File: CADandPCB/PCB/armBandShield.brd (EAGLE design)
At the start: 26.1 x 55.9 mm, 33 parts, among them J1 FSR_HEADERS_1, J2 FSR_HEADERS_2, Q1 BSS138, Q2 BSS138, U2 MPU-6050-1

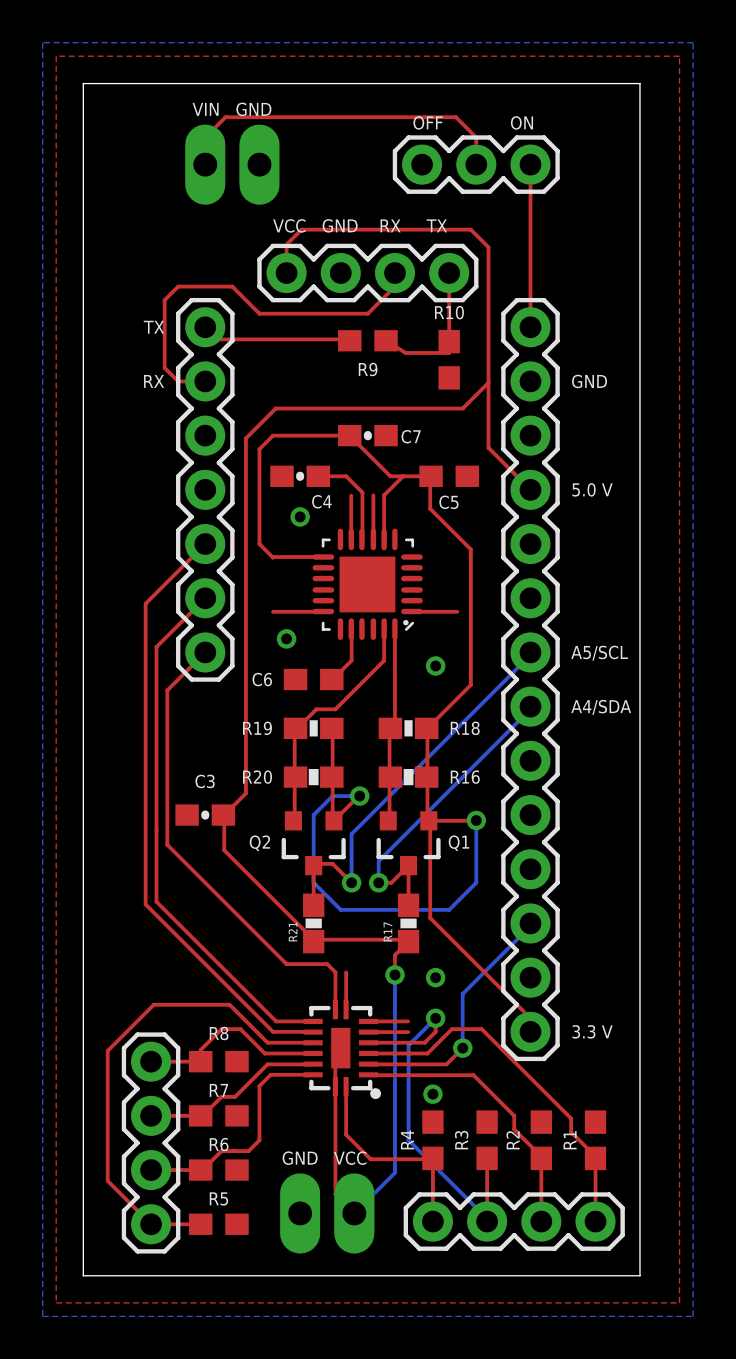
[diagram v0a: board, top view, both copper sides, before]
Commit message: Update trace sizes, pad extensions, silkscreen, and some routing.
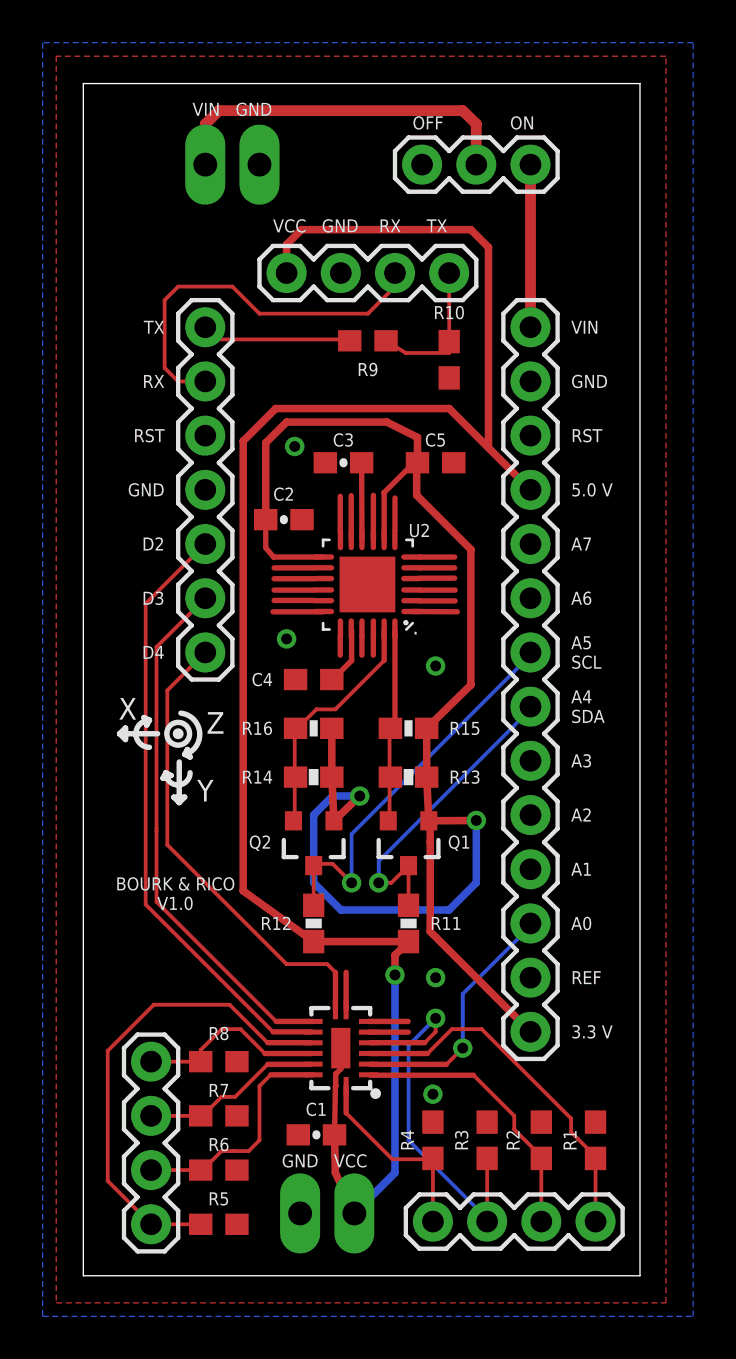
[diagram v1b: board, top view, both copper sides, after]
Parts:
- removed C6: 2.2nF, SparkFun-Capacitors:0603
- removed C7: 0.1uF, SparkFun-Capacitors:0603-CAP
- removed R19: 10K, SparkFun-Resistors:0603-RES
- added C1, C2: 0.1uF, SparkFun-Capacitors:0603-CAP
- added R13: 10K, SparkFun:0603-RES
- C4: value 0.1uF -> 2.2nF; device SparkFun-Capacitors:0603-CAP -> SparkFun-Capacitors:0603
- R16: device SparkFun:0603-RES -> SparkFun-Resistors:0603-RES
- moved C3 17.7 mm to (12.2, 38.1)
- moved C4 9.55 mm to (10.8, 27.9)
- moved R16 5.00 mm to (10.8, 25.7)
- moved C5 0.90 mm to (16.5, 38.1)
- renumbered R17 to R11, R18 to R15, R20 to R14, R21 to R12
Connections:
- net A4/SDA/LOW: now also R13.2; no longer R16.2
- net A5/SCL/LOW: now also R16.2; no longer R19.2
- net GND: now also C1.2, C2.2; no longer C6.2, C7.2
- net N$3: now also C4.1; no longer C6.1
- net N$5: now also C3.1; no longer C4.1
- net VCC: now also C1.1; no longer C3.1
- net VCC_2: now also C2.1, R13.1; no longer C7.1, R19.1
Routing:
- net VCC_2: track 75.6 -> 78.0 mm
- net N$9: track 0.00 -> 1.91 mm
- net N$8: track 0.00 -> 1.91 mm
- net N$6: track 0.00 -> 1.91 mm
- net N$4: track 0.00 -> 1.91 mm
- net N$16: track 0.00 -> 1.65 mm
- net N$15: track 0.00 -> 1.65 mm
- net N$14: track 0.00 -> 1.65 mm
- net N$17: track 0.00 -> 1.65 mm
- net N$13: track 0.00 -> 1.65 mm
- net N$19: track 0.00 -> 1.65 mm
- net N$18: track 0.00 -> 1.52 mm
- net N$5: track 4.59 -> 3.59 mm
- net N$1: track 16.0 -> 17.0 mm
- net N$12: track 0.00 -> 0.89 mm
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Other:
- board text added: "."
- board text added: "A0"
- board text added: "A1"
- board text added: "A2"
- board text added: "A3"
- board text added: "A4 SDA"
- board text added: "A5 SCL"
- board text added: "A6"
- board text added: "A7"
- board text added: "BOURK & RICO V1.0"
- board text added: "D2"
- board text added: "D3"
- board text added: "D4"
- board text added: "REF"
- board text added: "RST"
- board text added: "U2"
- board text added: "VIN"
- board text added: "X"
- board text added: "Y"
- board text added: "Z"
- board text removed: "A4/SDA"
- board text removed: "A5/SCL"

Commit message: Double checked schematic and moved a few traces for asthetics.
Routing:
- net VCC: track 88.3 -> 93.4 mm
- net VCC_2: track 78.0 -> 77.1 mm
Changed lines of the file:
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@@
 <circle x="4.445" y="25.4" radius="0.127" width="0.254" layer="21"/>
 <circle x="4.445" y="25.4" radius="0.5334" width="0.254" layer="21"/>
-<text x="4.318" y="17.145" size="0.6096" layer="25" font="vector" ratio="20" align="bottom-center">BOURK &amp; RICO
+<text x="3.683" y="14.605" size="0.6096" layer="25" font="vector" ratio="20" align="bottom-center">BOURK &amp; RICO
 V1.0</text>
 <text x="15.5702" y="30.4292" size="0.762" layer="25" font="vector" ratio="20" align="center">.</text>
@@
 <wire x1="13.5925" y1="34.5066" x2="13.5925" y2="36.5725" width="0.254" layer="1"/>
 <wire x1="12.5554" y1="34.5066" x2="12.5554" y2="36.5584" width="0.254" layer="1"/>
-<via x="16.383" y="8.509" extent="1-16" drill="0.508"/>
-<via x="16.51" y="13.97" extent="1-16" drill="0.508"/>
+<via x="17.653" y="8.509" extent="1-16" drill="0.508"/>
+<via x="15.24" y="13.97" extent="1-16" drill="0.508"/>
 <wire x1="11.2355" y1="31.115" x2="8.89" y2="31.115" width="0.254" layer="1"/>
 <contactref element="U2" pad="9"/>
@@
 <wire x1="9.525" y1="48.3235" x2="9.525" y2="46.99" width="0.3556" layer="1"/>
 <wire x1="7.493" y1="18.034" x2="7.493" y2="39.116" width="0.3556" layer="1"/>
-<wire x1="14.605" y1="14.097" x2="14.605" y2="4.826" width="0.3556" layer="16"/>
-<wire x1="14.605" y1="4.826" x2="12.7" y2="2.921" width="0.3556" layer="16"/>
-<wire x1="14.605" y1="15.025" x2="14.605" y2="14.097" width="0.3556" layer="1"/>
-<via x="14.605" y="14.097" extent="1-16" drill="0.508"/>
+<via x="7.493" y="18.034" extent="1-16" drill="0.508"/>
 <wire x1="20.955" y1="36.83" x2="18.9865" y2="38.7985" width="0.3556" layer="1"/>
 <wire x1="18.9865" y1="38.7985" x2="17.145" y2="40.64" width="0.3556" layer="1"/>
@@
 <wire x1="17.145" y1="40.64" x2="9.017" y2="40.64" width="0.3556" layer="1"/>
 <wire x1="18.9865" y1="38.7985" x2="18.9865" y2="48.1965" width="0.3556" layer="1"/>
-<wire x1="10.795" y1="15.66" x2="7.493" y2="18.034" width="0.3556" layer="1"/>
-<wire x1="11.9086" y1="6.7406" x2="11.772" y2="6.604" width="0.3556" layer="1"/>
-<wire x1="11.772" y1="6.604" x2="11.7816" y2="6.763109375" width="0.3556" layer="1"/>
 <wire x1="10.795" y1="15.66" x2="15.24" y2="15.66" width="0.3556" layer="1"/>
-<wire x1="15.24" y1="15.66" x2="14.605" y2="15.025" width="0.3556" layer="1"/>
 <wire x1="12.7" y1="2.921" x2="11.811" y2="4.826" width="0.3556" layer="1"/>
 <wire x1="11.811" y1="4.826" x2="11.772" y2="6.604" width="0.3556" layer="1"/>
@@
 <wire x1="12.065" y1="9.69089375" x2="11.8324" y2="9.45829375" width="0.254" layer="1"/>
 <wire x1="11.8324" y1="9.45829375" x2="11.8324" y2="8.8854" width="0.254" layer="1"/>
+<wire x1="7.493" y1="18.034" x2="10.795" y2="15.66" width="0.3556" layer="1"/>
+<wire x1="7.493" y1="18.034" x2="14.6304" y2="12.9286" width="0.3556" layer="16"/>
+<wire x1="14.6304" y1="12.9286" x2="14.605" y2="6.35" width="0.3556" layer="16"/>
+<wire x1="14.605" y1="6.35" x2="12.7" y2="2.921" width="0.3556" layer="16"/>
 </signal>
 <signal name="RX">
@@
 <contactref element="RIGHT_HEADER" pad="1"/>
 <wire x1="16.256" y1="16.129" x2="20.955" y2="11.43" width="0.3556" layer="1"/>
-<wire x1="16.256" y1="21.209" x2="16.256" y2="20.32" width="0.3556" layer="1"/>
-<wire x1="16.256" y1="20.32" x2="16.256" y2="16.129" width="0.3556" layer="1"/>
+<wire x1="16.256" y1="16.129" x2="16.256" y2="20.32" width="0.3556" layer="1"/>
 <wire x1="15.494" y1="38.1" x2="15.66" y2="38.1" width="0.254" layer="1"/>
 <wire x1="18.161" y1="34.036" x2="15.621" y2="36.576" width="0.3556" layer="1"/>
@@
 <wire x1="16.19" y1="21.32" x2="16.09" y2="23.368" width="0.3556" layer="1"/>
 <wire x1="16.19" y1="21.32" x2="18.415" y2="21.336" width="0.3556" layer="1"/>
-<wire x1="16.19" y1="21.32" x2="16.256" y2="20.32" width="0.254" layer="1"/>
+<wire x1="16.256" y1="20.32" x2="16.19" y2="21.32" width="0.3556" layer="1"/>
 </signal>
 <signal name="A5/SCL/HIGH">

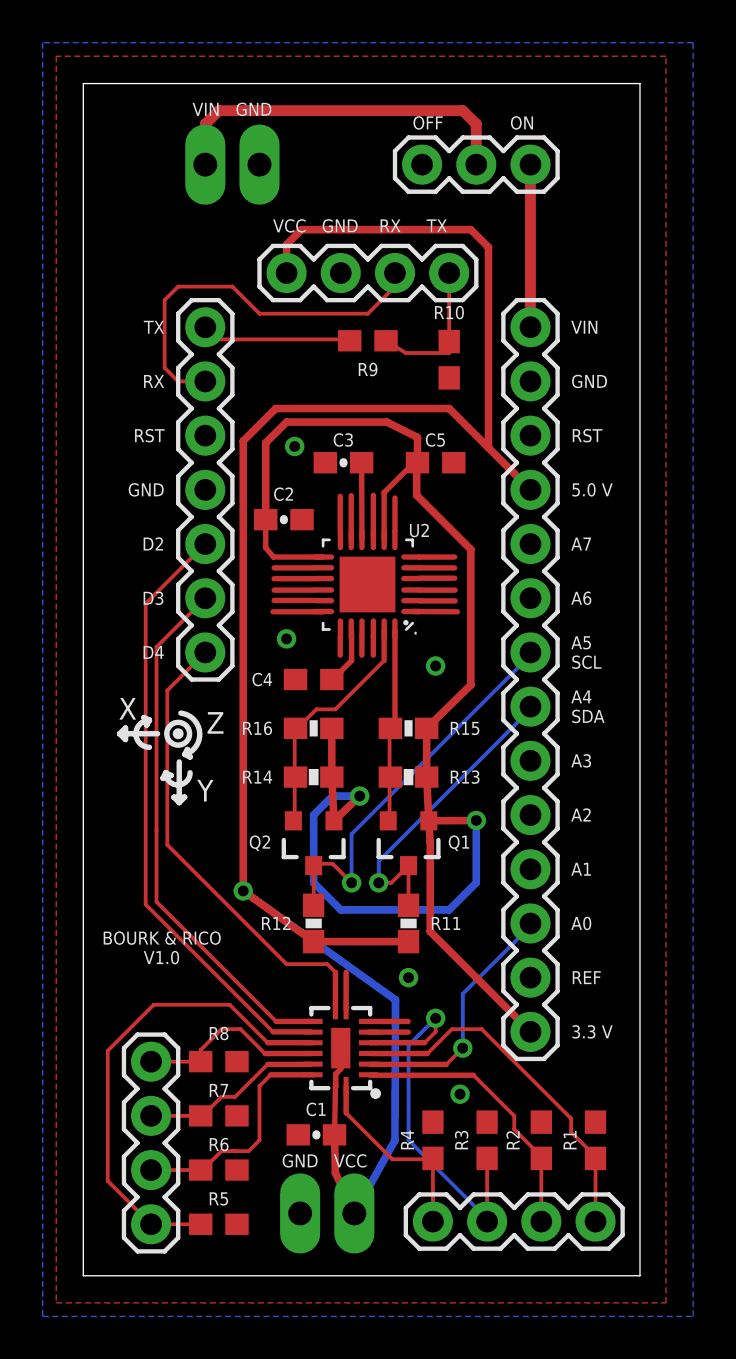
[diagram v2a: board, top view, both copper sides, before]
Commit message: Increase tstop and tcream
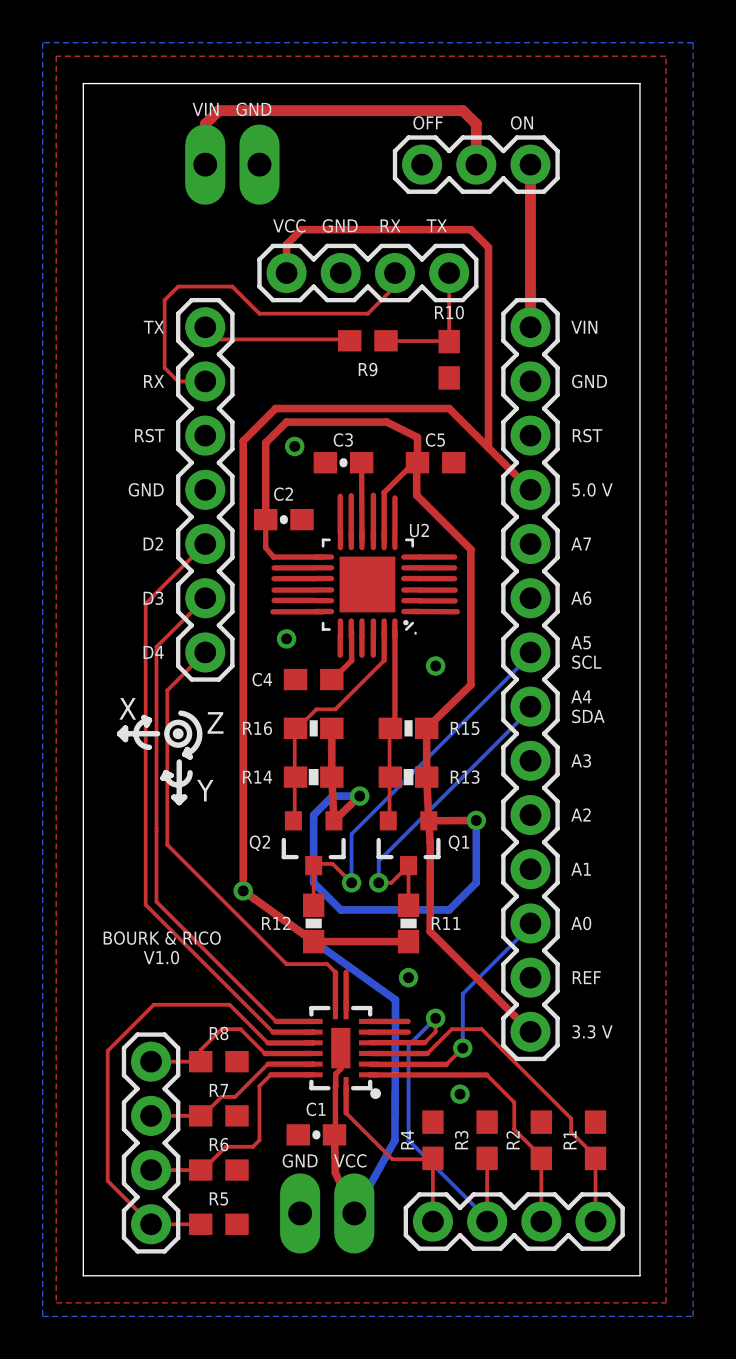
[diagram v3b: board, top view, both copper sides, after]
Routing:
- net N$7: track 6.87 -> 6.19 mm

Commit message: Commit Gerber files and final rev 1 of board.
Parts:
- removed SWITCH_HEADERS: J8, SparkFun-Connectors:1X03
- added J10, J8, J9: (no value), SparkFun-Connectors:1X01
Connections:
- net N$1: now also J9.1; no longer SWITCH_HEADERS.2
- net VIN: now also J10.1; no longer SWITCH_HEADERS.1
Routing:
- net N$1: track 17.0 -> 15.2 mm
- net VIN: track 7.62 -> 6.98 mm
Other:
- board text added: "5 V"
- board text removed: "."
- board text removed: "5.0 V"
